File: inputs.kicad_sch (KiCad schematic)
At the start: 16 parts

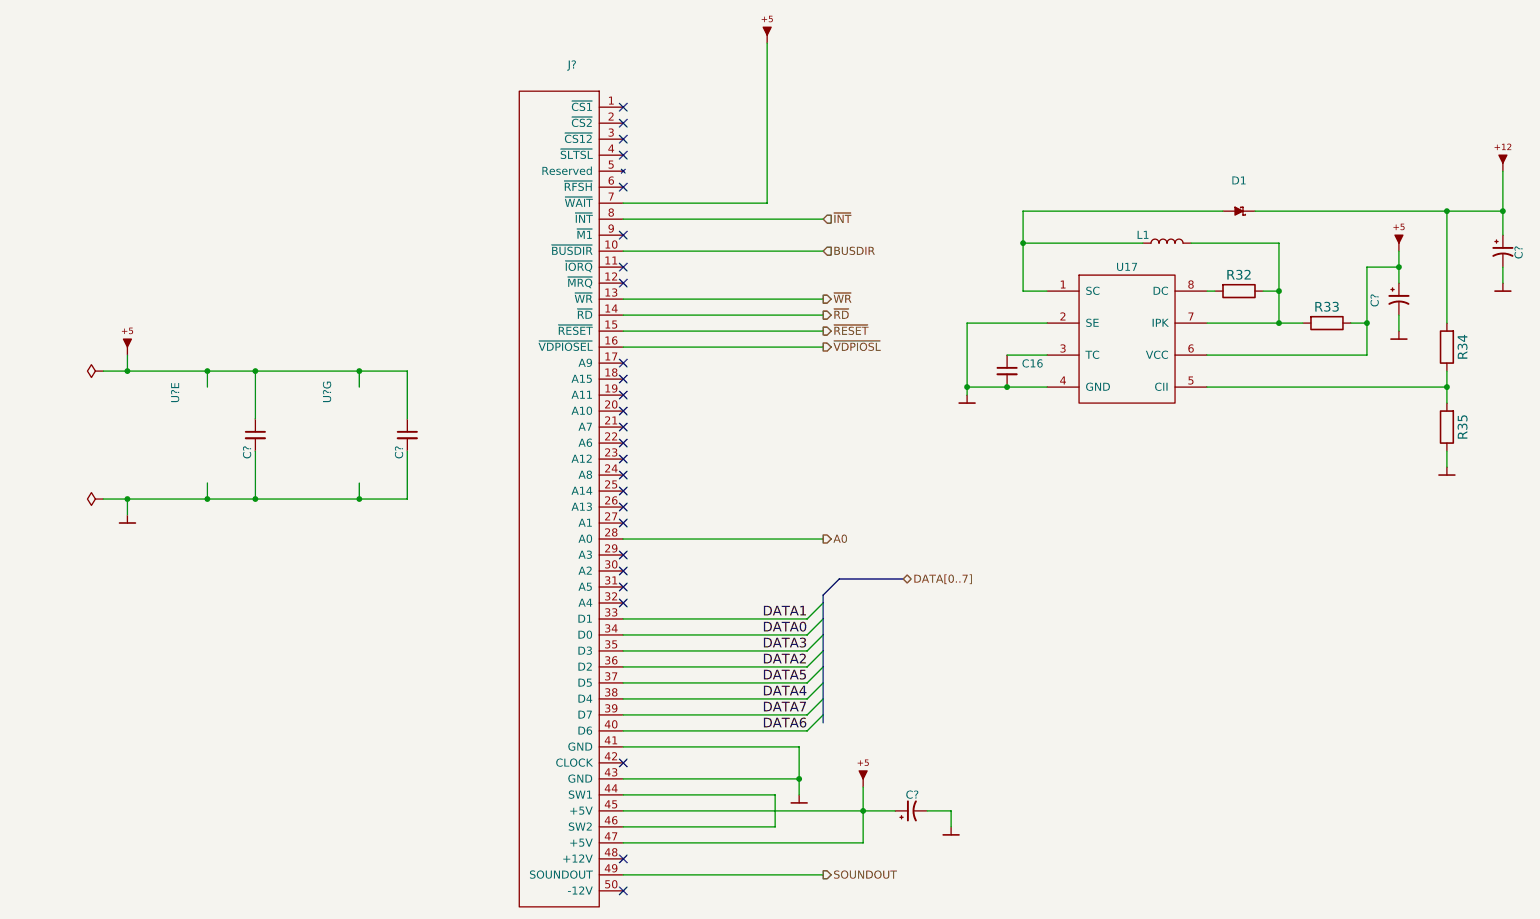
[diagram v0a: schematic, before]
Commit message: Migrate to KiCad v8
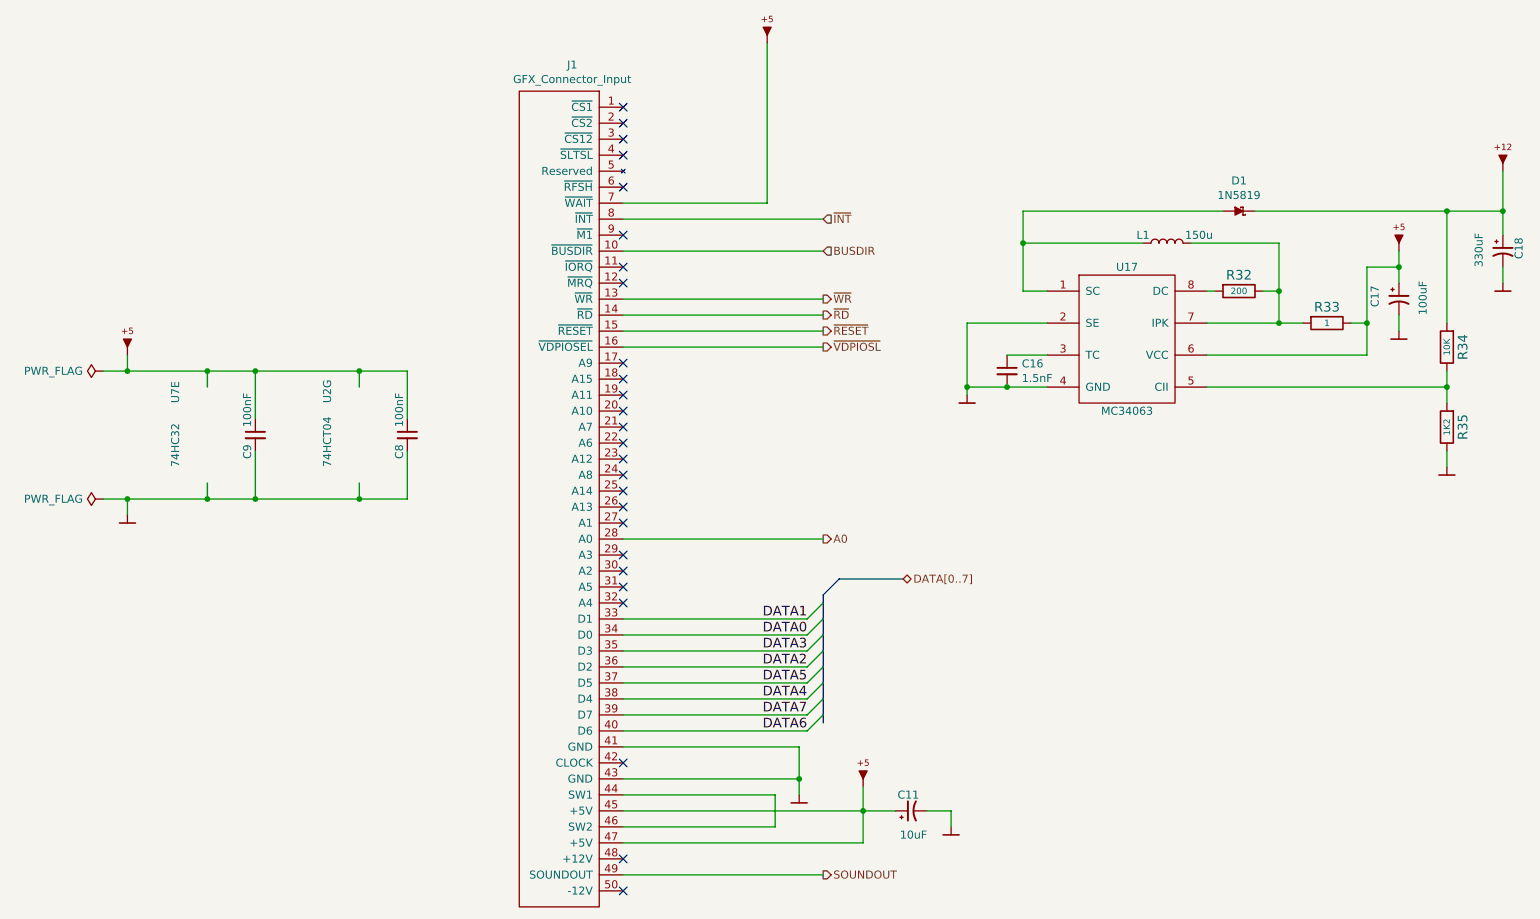
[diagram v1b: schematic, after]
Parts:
- C11: renamed from C?; value (none) -> 10uF; footprint (none) -> artemisa:Radial_capacitor
- C16: value (none) -> 1.5nF
- C17: renamed from C?; value (none) -> 100uF; footprint (none) -> artemisa:Radial_capacitor
- C18: renamed from C?; value (none) -> 330uF; footprint (none) -> artemisa:Radial_capacitor
- C8, C9: renamed from C?; value (none) -> 100nF; footprint (none) -> artemisa:Disc_capacitor
- D1: value (none) -> 1N5819
- J1: renamed from J?; value (none) -> GFX_Connector_Input; footprint (none) -> artemisa:GFX_conn
- L1: value (none) -> 150u
- R32: value (none) -> 200
- R33: value (none) -> 1
- R34: value (none) -> 10K
- R35: value (none) -> 1K2
- U17: value (none) -> MC34063
- U2: renamed from U?; value (none) -> 74HCT04; footprint (none) -> artemisa:DIP-14_300
- U7: renamed from U?; value (none) -> 74HC32; footprint (none) -> artemisa:DIP-14_300
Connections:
- net +12V renamed 12V
